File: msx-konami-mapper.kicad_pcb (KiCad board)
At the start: 2 copper layers, 65.3 x 63 mm, 12 parts, among them SW1 Bonus Games, U1 SST39SF040, U3 74LS670, U4 74LS02

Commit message: Add 'rear' tag
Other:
- board text added: "rear"
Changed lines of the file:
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@@
 	)
 	(gr_text "MSX rules"
-		(at 147.955 52.07 0)
+		(at 140.97 52.07 0)
 		(layer "B.SilkS")
 		(effects
+			(font
+				(size 1 1)
+				(thickness 0.1)
+			)
+			(justify right bottom mirror)
+		)
+	)
+	(gr_text "rear"
+		(at 204.47 51.435 0)
+		(layer "B.SilkS")
+		(effects

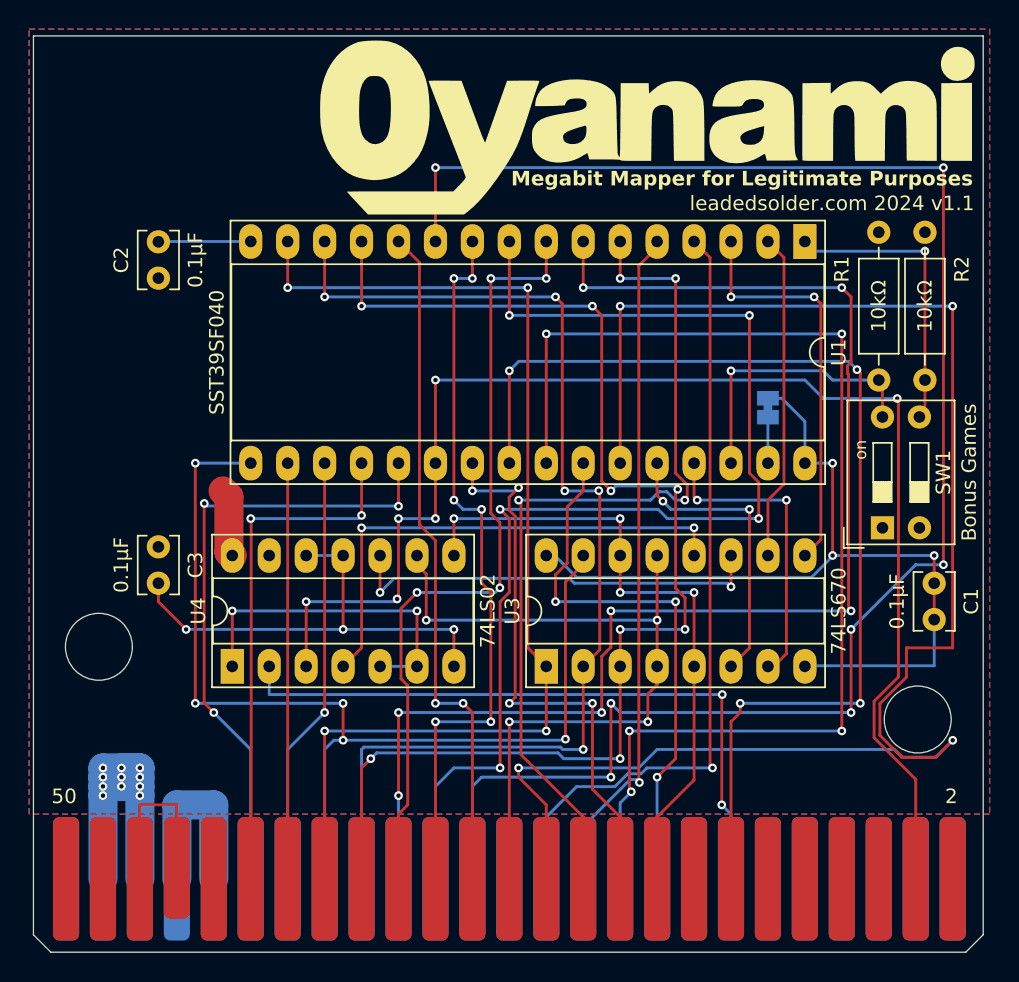
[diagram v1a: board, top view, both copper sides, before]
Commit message: Pull-downs for '670 output
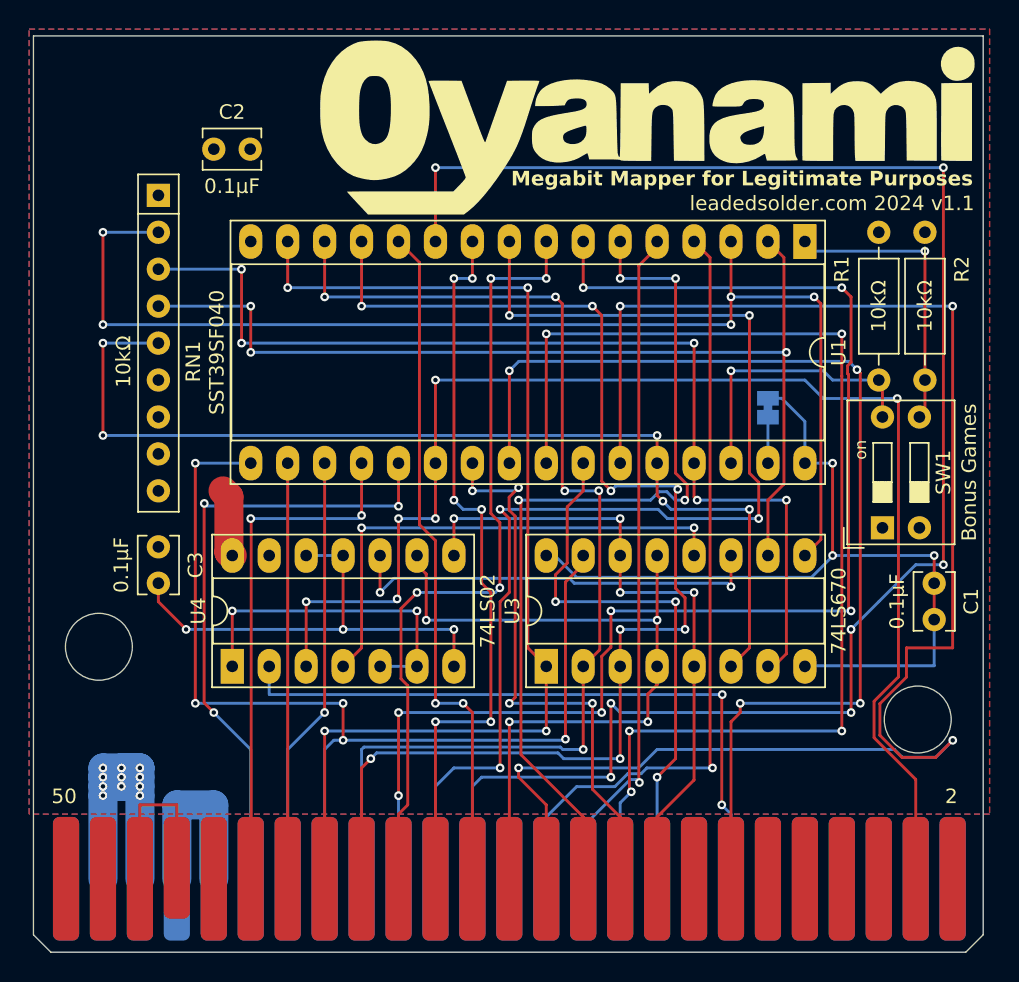
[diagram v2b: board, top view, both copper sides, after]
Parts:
- added RN1: 10kΩ, Resistor_THT:R_Array_SIP9, F.Cu at (148.6, 61.0)
- moved C2 9.65 mm to (152.4, 57.8), turned to 0 degrees
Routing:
- net /PA15: track 28.0 -> 83.2 mm, vias 2 -> 5
- net /PA13: track 20.3 -> 70.4 mm, vias 2 -> 5
- net /PA14: track 21.0 -> 71.1 mm, vias 2 -> 5
- net /PA16: track 22.5 -> 69.0 mm, vias 0 -> 3
- net GND: track 63.7 -> 57.3 mm

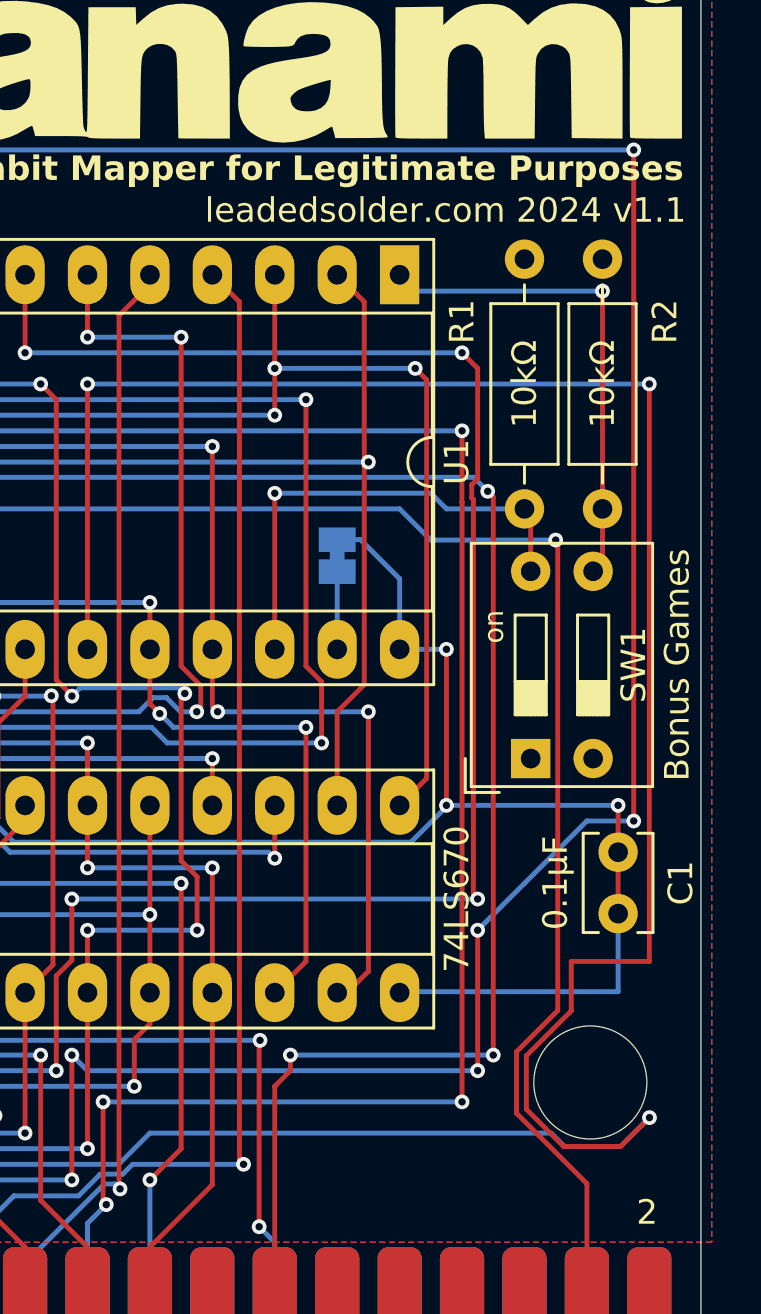
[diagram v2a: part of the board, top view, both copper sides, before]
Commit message: Fix DIP switch being backward
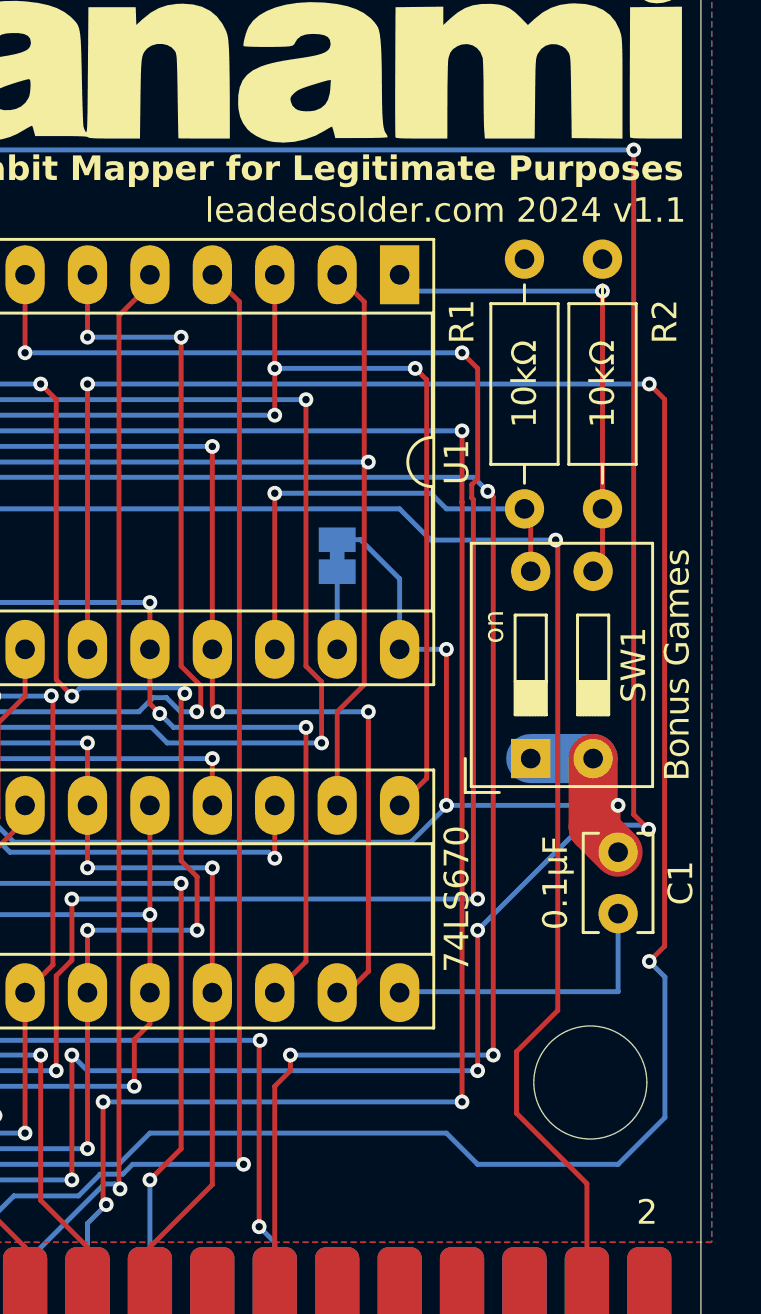
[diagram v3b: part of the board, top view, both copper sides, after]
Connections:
- R1 pad 1: +5V -> GND
- R2 pad 1: +5V -> GND
- SW1 pad 1: GND -> +5V
- SW1 pad 2: GND -> +5V
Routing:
- net /A8: track 112.7 -> 105.0 mm
- net +5V: track 73.8 -> 77.4 mm
- net /A1: track 119.2 -> 120.4 mm
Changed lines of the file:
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@@
 			(layers "*.Cu" "*.Mask")
 			(remove_unused_layers no)
-			(net 48 "GND")
+			(net 43 "+5V")
 			(pintype "passive")
 		)
@@
 			(layers "*.Cu" "*.Mask")
 			(remove_unused_layers no)
-			(net 48 "GND")
+			(net 43 "+5V")
 			(pintype "passive")
 		)
@@
 			(layers "*.Cu" "*.Mask")
 			(remove_unused_layers no)
-			(net 43 "+5V")
+			(net 48 "GND")
 			(pintype "passive")
 		)
@@
 			(layers "*.Cu" "*.Mask")
 			(remove_unused_layers no)
-			(net 43 "+5V")
+			(net 48 "GND")
 			(pintype "passive")
 		)
@@
 	)
 	(segment
-		(start 202.565 86.36)
-		(end 202.565 59.055)
+		(start 202.565 86.095077)
+		(end 203.170234 86.700311)
+		(width 0.2)
+		(layer "F.Cu")
+		(net 26)
+	)
+	(segment
+		(start 202.565 59.055)
+		(end 202.565 86.095077)
 		(width 0.2)
 		(layer "F.Cu")
@@
 	)
 	(via
-		(at 202.565 86.36)
+		(at 203.170234 86.700311)
 		(size 0.6)
 		(drill 0.3)
@@
 	)
 	(segment
-		(start 198.12 88.9)
-		(end 200.66 86.36)
+		(start 179.705 95.885)
+		(end 180.34 96.52)
 		(width 0.2)
 		(layer "B.Cu")
@@
 	)
 	(segment
-		(start 179.705 95.885)
-		(end 180.34 96.52)
+		(start 196.215 90.805)
+		(end 200.49 86.53)
 		(width 0.2)
 		(layer "B.Cu")
@@
 	)
 	(segment
-		(start 196.215 90.805)
-		(end 198.12 88.9)
+		(start 200.49 86.53)
+		(end 202.999923 86.53)
 		(width 0.2)
 		(layer "B.Cu")
@@
 	)
 	(segment
-		(start 200.66 86.36)
-		(end 202.565 86.36)
+		(start 202.999923 86.53)
+		(end 203.170234 86.700311)
 		(width 0.2)
 		(layer "B.Cu")
@@
 	)
 	(segment
-		(start 200.025 92.075)
-		(end 203.2 92.075)
-		(width 0.2)
-		(layer "F.Cu")
-		(net 28)
-	)
-	(segment
-		(start 198.197548 98.087372)
-		(end 198.197548 95.912628)
+		(start 203.820234 91.454766)
+		(end 203.820234 69.200234)
 		(width 0.2)
 		(layer "F.Cu")
@@
 	(segment
 		(start 203.2 92.075)
-		(end 203.2 68.58)
-		(width 0.2)
-		(layer "F.Cu")
-		(net 28)
-	)
-	(segment
-		(start 198.197548 95.912628)
-		(end 200.025 94.085176)
-		(width 0.2)
-		(layer "F.Cu")
-		(net 28)
-	)
-	(segment
-		(start 202.033759 99.602452)
-		(end 199.712628 99.602452)
+		(end 203.820234 91.454766)
 		(width 0.2)
 		(layer "F.Cu")
@@
 	)
 	(segment
-		(start 175.26 102.87)
-		(end 173.355 100.965)
-		(width 0.2)
-		(layer "F.Cu")
-		(net 28)
-	)
-	(segment
-		(start 200.025 94.085176)
-		(end 200.025 92.075)
-		(width 0.2)
-		(layer "F.Cu")
-		(net 28)
-	)
-	(segment
-		(start 203.206551 98.42966)
-		(end 202.033759 99.602452)
+		(start 203.820234 69.200234)
+		(end 203.2 68.58)
 		(width 0.2)
 		(layer "F.Cu")
@@
 	)
 	(segment
-		(start 199.712628 99.602452)
-		(end 198.197548 98.087372)
+		(start 175.26 102.87)
+		(end 173.355 100.965)
 		(width 0.2)
 		(layer "F.Cu")
@@
 	)
 	(via
-		(at 203.206551 98.42966)
+		(at 173.355 100.33)
 		(size 0.6)
 		(drill 0.3)
@@
 	)
 	(via
-		(at 173.355 100.33)
+		(at 203.2 92.075)
 		(size 0.6)
 		(drill 0.3)
@@
 	)
 	(segment
-		(start 199.745766 99.602452)
-		(end 202.033759 99.602452)
+		(start 194.945 99.06)
+		(end 196.215 100.33)
 		(width 0.2)
 		(layer "B.Cu")
@@
 	)
 	(segment
-		(start 199.203314 99.06)
-		(end 199.745766 99.602452)
+		(start 203.835 98.425)
+		(end 203.835 92.71)
+		(width 0.2)
+		(layer "B.Cu")
+		(net 28)
+	)
+	(segment
+		(start 201.93 100.33)
+		(end 203.835 98.425)
 		(width 0.2)
 		(layer "B.Cu")
@@
 	)
 	(segment
-		(start 182.88 99.06)
-		(end 199.203314 99.06)
+		(start 203.835 92.71)
+		(end 203.2 92.075)
 		(width 0.2)
 		(layer "B.Cu")
@@
 	)
 	(segment
-		(start 202.033759 99.602452)
-		(end 203.206551 98.42966)
+		(start 196.215 100.33)
+		(end 201.93 100.33)
+		(width 0.2)
+		(layer "B.Cu")
+		(net 28)
+	)
+	(segment
+		(start 182.88 99.06)
+		(end 194.945 99.06)
 		(width 0.2)
 		(layer "B.Cu")
@@
 	)
 	(segment
+		(start 201.93 87.63)
+		(end 201.93 85.725)
+		(width 0.2)
+		(layer "F.Cu")
+		(net 43)
+	)
+	(segment
 		(start 153.44 81.685)
 		(end 153.035 81.28)
@@
 	)
 	(segment
-		(start 201.93 90.805)
-		(end 201.93 85.725)
-		(width 0.2)
+		(start 200.914 86.614)
+		(end 201.93 87.63)
+		(width 2)
 		(layer "F.Cu")
 		(net 43)
@@
 		(net 43)
 	)
+	(segment
+		(start 200.914 83.82)
+		(end 200.914 86.614)
+		(width 2)
+		(layer "F.Cu")
+		(net 43)
+	)
 	(via
 		(at 144.78 100.965)
@@
 		(layer "B.Cu")
 		(net 43)
+	)
+	(segment
+		(start 200.914 83.82)
+		(end 198.374 83.82)
+		(width 2)
+		(layer "B.Cu")
+		(net 43)
